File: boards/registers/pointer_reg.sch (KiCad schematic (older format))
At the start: 80 parts

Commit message: General-purpose register
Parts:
- U? (x4): value 74HC244 -> 74ACT244
- U? (x4): value 74LS161 -> 74ACT161
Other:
- note added: "The resistor values are such that each LED is driven by 10 mA (prevent 74ACT161 overload)."
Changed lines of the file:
@@
 $Descr A3 11693 16535 portrait
 encoding utf-8
-Sheet 3 4
+Sheet 3 6
 Title "Pointer register"
 Date "2019-12-28"
@@
 AR Path="/5E0666E8/5E5C90D9/5E067470" Ref="U?"  Part="1"
 F 0 "U?" H 5950 3250 50  0000 C CNN
-F 1 "74HC244" H 5850 3150 50  0000 C CNN
+F 1 "74ACT244" H 5850 3150 50  0000 C CNN
 F 2 "" H 5550 3850 50  0001 C CNN
 F 3 "https://assets.nexperia.com/documents/data-sheet/74HC_HCT244.pdf" H 5550 3850 50  0001 C CNN
@@
 AR Path="/5E0666E8/5E5C90D9/5E06F6F1" Ref="U?"  Part="1"
 F 0 "U?" H 8700 3200 50  0000 C CNN
-F 1 "74HC244" H 8600 3100 50  0000 C CNN
+F 1 "74ACT244" H 8600 3100 50  0000 C CNN
 F 2 "" H 8300 3850 50  0001 C CNN
 F 3 "https://assets.nexperia.com/documents/data-sheet/74HC_HCT244.pdf" H 8300 3850 50  0001 C CNN
@@
 AR Path="/5E0666E8/5E5C90D9/5E07142A" Ref="U?"  Part="1"
 F 0 "U?" H 5950 5900 50  0000 C CNN
-F 1 "74HC244" H 5850 5800 50  0000 C CNN
+F 1 "74ACT244" H 5850 5800 50  0000 C CNN
 F 2 "" H 5550 6500 50  0001 C CNN
 F 3 "https://assets.nexperia.com/documents/data-sheet/74HC_HCT244.pdf" H 5550 6500 50  0001 C CNN
@@
 AR Path="/5E0666E8/5E5C90D9/5E072984" Ref="U?"  Part="1"
 F 0 "U?" H 8650 5900 50  0000 C CNN
-F 1 "74HC244" H 8550 5800 50  0000 C CNN
+F 1 "74ACT244" H 8550 5800 50  0000 C CNN
 F 2 "" H 8250 6500 50  0001 C CNN
 F 3 "https://assets.nexperia.com/documents/data-sheet/74HC_HCT244.pdf" H 8250 6500 50  0001 C CNN
@@
 AR Path="/5E0666E8/5E5C90D9/5E0E2189" Ref="U?"  Part="1"
 F 0 "U?" H 4250 8700 50  0000 C CNN
-F 1 "74LS161" H 4150 8600 50  0000 C CNN
+F 1 "74ACT161" H 4150 8600 50  0000 C CNN
 F 2 "" H 3850 9250 50  0001 C CNN
 F 3 "http://www.ti.com/lit/gpn/sn74LS161" H 3850 9250 50  0001 C CNN
@@
 AR Path="/5E0666E8/5E5C90D9/5E0E857B" Ref="U?"  Part="1"
 F 0 "U?" H 4250 10850 50  0000 C CNN
-F 1 "74LS161" H 4150 10750 50  0000 C CNN
+F 1 "74ACT161" H 4150 10750 50  0000 C CNN
 F 2 "" H 3850 11400 50  0001 C CNN
 F 3 "http://www.ti.com/lit/gpn/sn74LS161" H 3850 11400 50  0001 C CNN
@@
 AR Path="/5E0666E8/5E5C90D9/5E0E941D" Ref="U?"  Part="1"
 F 0 "U?" H 6950 8700 50  0000 C CNN
-F 1 "74LS161" H 6850 8600 50  0000 C CNN
+F 1 "74ACT161" H 6850 8600 50  0000 C CNN
 F 2 "" H 6550 9250 50  0001 C CNN
 F 3 "http://www.ti.com/lit/gpn/sn74LS161" H 6550 9250 50  0001 C CNN
@@
 AR Path="/5E0666E8/5E5C90D9/5E0EB83E" Ref="U?"  Part="1"
 F 0 "U?" H 6950 10800 50  0000 C CNN
-F 1 "74LS161" H 6850 10700 50  0000 C CNN
+F 1 "74ACT161" H 6850 10700 50  0000 C CNN
 F 2 "" H 6550 11350 50  0001 C CNN
 F 3 "http://www.ti.com/lit/gpn/sn74LS161" H 6550 11350 50  0001 C CNN
@@
 Text Label 5100 14600 2    50   ~ 0
 lo7
+Text Notes 10700 13600 2    50   ~ 0
+The resistor values are such that each LED is driven by 10 mA (prevent 74ACT161 overload).
 $EndSCHEMATC

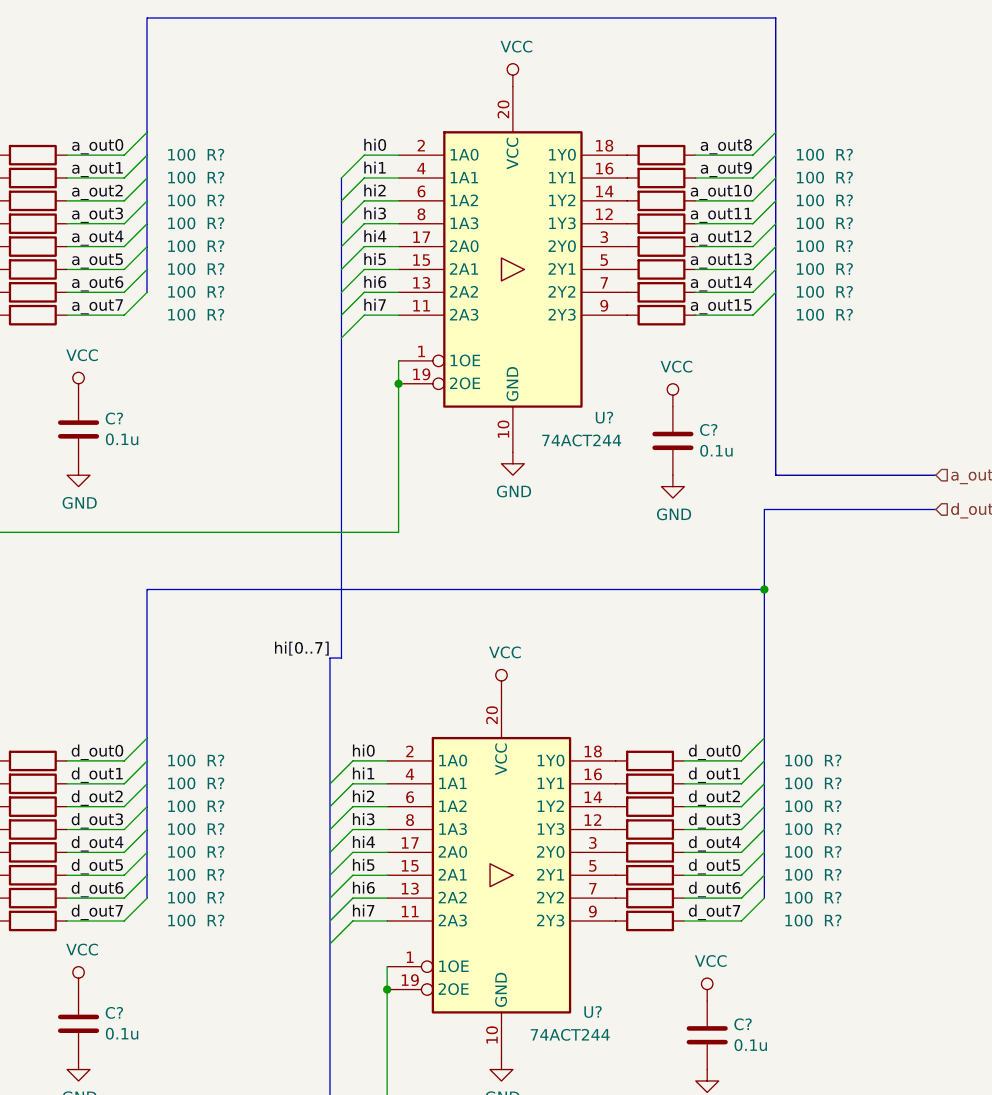
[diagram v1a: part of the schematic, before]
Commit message: Add bus resistors
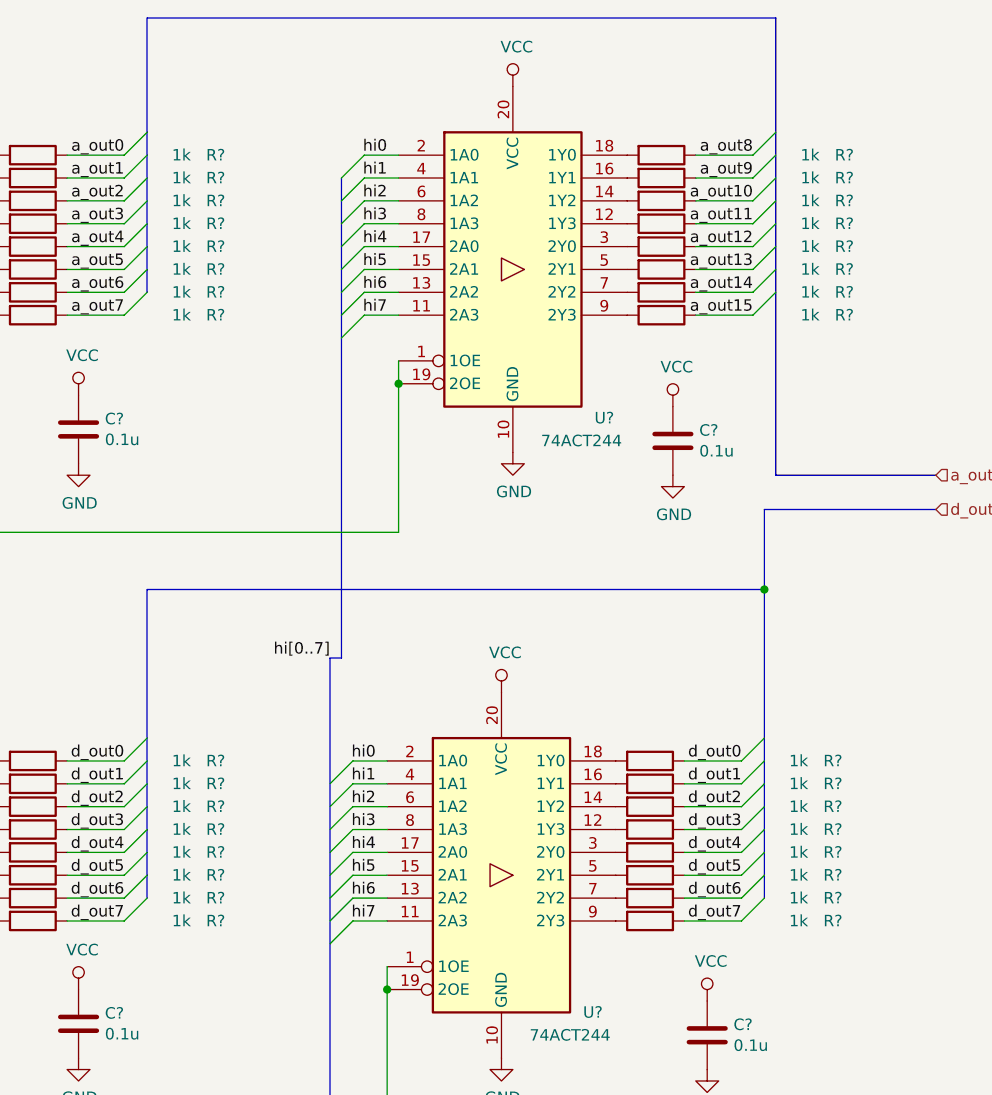
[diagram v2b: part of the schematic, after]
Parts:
- R? (x32): value 100 -> 1k
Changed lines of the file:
@@
 AR Path="/5E0666E8/5E5C90D9/5E079467" Ref="R?"  Part="1"
 F 0 "R?" V 6200 4150 50  0000 C CNN
-F 1 "100" V 6200 4000 50  0000 C CNN
+F 1 "1k" V 6200 4000 50  0000 C CNN
 F 2 "" V 6130 3350 50  0001 C CNN
 F 3 "~" H 6200 3350 50  0001 C CNN
@@
 AR Path="/5E0666E8/5E5C90D9/5E07A82D" Ref="R?"  Part="1"
 F 0 "R?" V 6200 4250 50  0000 C CNN
-F 1 "100" V 6200 4100 50  0000 C CNN
+F 1 "1k" V 6200 4100 50  0000 C CNN
 F 2 "" V 6130 3450 50  0001 C CNN
 F 3 "~" H 6200 3450 50  0001 C CNN
@@
 AR Path="/5E0666E8/5E5C90D9/5E07AA0F" Ref="R?"  Part="1"
 F 0 "R?" V 6200 4350 50  0000 C CNN
-F 1 "100" V 6200 4200 50  0000 C CNN
+F 1 "1k" V 6200 4200 50  0000 C CNN
 F 2 "" V 6130 3550 50  0001 C CNN
 F 3 "~" H 6200 3550 50  0001 C CNN
@@
 AR Path="/5E0666E8/5E5C90D9/5E07AB88" Ref="R?"  Part="1"
 F 0 "R?" V 6200 4450 50  0000 C CNN
-F 1 "100" V 6200 4300 50  0000 C CNN
+F 1 "1k" V 6200 4300 50  0000 C CNN
 F 2 "" V 6130 3650 50  0001 C CNN
 F 3 "~" H 6200 3650 50  0001 C CNN
@@
 AR Path="/5E0666E8/5E5C90D9/5E07AE3C" Ref="R?"  Part="1"
 F 0 "R?" V 6200 4550 50  0000 C CNN
-F 1 "100" V 6200 4400 50  0000 C CNN
+F 1 "1k" V 6200 4400 50  0000 C CNN
 F 2 "" V 6130 3750 50  0001 C CNN
 F 3 "~" H 6200 3750 50  0001 C CNN
@@
 AR Path="/5E0666E8/5E5C90D9/5E07B009" Ref="R?"  Part="1"
 F 0 "R?" V 6200 4650 50  0000 C CNN
-F 1 "100" V 6200 4500 50  0000 C CNN
+F 1 "1k" V 6200 4500 50  0000 C CNN
 F 2 "" V 6130 3850 50  0001 C CNN
 F 3 "~" H 6200 3850 50  0001 C CNN
@@
 AR Path="/5E0666E8/5E5C90D9/5E07B2BD" Ref="R?"  Part="1"
 F 0 "R?" V 6200 4750 50  0000 C CNN
-F 1 "100" V 6200 4600 50  0000 C CNN
+F 1 "1k" V 6200 4600 50  0000 C CNN
 F 2 "" V 6130 3950 50  0001 C CNN
 F 3 "~" H 6200 3950 50  0001 C CNN
@@
 AR Path="/5E0666E8/5E5C90D9/5E07B51D" Ref="R?"  Part="1"
 F 0 "R?" V 6200 4850 50  0000 C CNN
-F 1 "100" V 6200 4700 50  0000 C CNN
+F 1 "1k" V 6200 4700 50  0000 C CNN
 F 2 "" V 6130 4050 50  0001 C CNN
 F 3 "~" H 6200 4050 50  0001 C CNN
@@
 AR Path="/5E0666E8/5E5C90D9/5E07B83A" Ref="R?"  Part="1"
 F 0 "R?" V 8950 4150 50  0000 C CNN
-F 1 "100" V 8950 4000 50  0000 C CNN
+F 1 "1k" V 8950 4000 50  0000 C CNN
 F 2 "" V 8880 3350 50  0001 C CNN
 F 3 "~" H 8950 3350 50  0001 C CNN
@@
 AR Path="/5E0666E8/5E5C90D9/5E07C172" Ref="R?"  Part="1"
 F 0 "R?" V 8950 4250 50  0000 C CNN
-F 1 "100" V 8950 4100 50  0000 C CNN
+F 1 "1k" V 8950 4100 50  0000 C CNN
 F 2 "" V 8880 3450 50  0001 C CNN
 F 3 "~" H 8950 3450 50  0001 C CNN
@@
 AR Path="/5E0666E8/5E5C90D9/5E07C354" Ref="R?"  Part="1"
 F 0 "R?" V 8950 4350 50  0000 C CNN
-F 1 "100" V 8950 4200 50  0000 C CNN
+F 1 "1k" V 8950 4200 50  0000 C CNN
 F 2 "" V 8880 3550 50  0001 C CNN
 F 3 "~" H 8950 3550 50  0001 C CNN
@@
 AR Path="/5E0666E8/5E5C90D9/5E07C50C" Ref="R?"  Part="1"
 F 0 "R?" V 8950 4450 50  0000 C CNN
-F 1 "100" V 8950 4300 50  0000 C CNN
+F 1 "1k" V 8950 4300 50  0000 C CNN
 F 2 "" V 8880 3650 50  0001 C CNN
 F 3 "~" H 8950 3650 50  0001 C CNN
@@
 AR Path="/5E0666E8/5E5C90D9/5E07C6AF" Ref="R?"  Part="1"
 F 0 "R?" V 8950 4550 50  0000 C CNN
-F 1 "100" V 8950 4400 50  0000 C CNN
+F 1 "1k" V 8950 4400 50  0000 C CNN
 F 2 "" V 8880 3750 50  0001 C CNN
 F 3 "~" H 8950 3750 50  0001 C CNN
@@
 AR Path="/5E0666E8/5E5C90D9/5E07C852" Ref="R?"  Part="1"
 F 0 "R?" V 8950 4650 50  0000 C CNN
-F 1 "100" V 8950 4500 50  0000 C CNN
+F 1 "1k" V 8950 4500 50  0000 C CNN
 F 2 "" V 8880 3850 50  0001 C CNN
 F 3 "~" H 8950 3850 50  0001 C CNN
@@
 AR Path="/5E0666E8/5E5C90D9/5E07C9CB" Ref="R?"  Part="1"
 F 0 "R?" V 8950 4750 50  0000 C CNN
-F 1 "100" V 8950 4600 50  0000 C CNN
+F 1 "1k" V 8950 4600 50  0000 C CNN
 F 2 "" V 8880 3950 50  0001 C CNN
 F 3 "~" H 8950 3950 50  0001 C CNN
@@
 AR Path="/5E0666E8/5E5C90D9/5E07CCA9" Ref="R?"  Part="1"
 F 0 "R?" V 8950 4850 50  0000 C CNN
-F 1 "100" V 8950 4700 50  0000 C CNN
+F 1 "1k" V 8950 4700 50  0000 C CNN
 F 2 "" V 8880 4050 50  0001 C CNN
 F 3 "~" H 8950 4050 50  0001 C CNN
@@
 AR Path="/5E0666E8/5E5C90D9/5E07CEB5" Ref="R?"  Part="1"
 F 0 "R?" V 6200 6800 50  0000 C CNN
-F 1 "100" V 6200 6650 50  0000 C CNN
+F 1 "1k" V 6200 6650 50  0000 C CNN
 F 2 "" V 6130 6000 50  0001 C CNN
 F 3 "~" H 6200 6000 50  0001 C CNN
@@
 AR Path="/5E0666E8/5E5C90D9/5E07D90A" Ref="R?"  Part="1"
 F 0 "R?" V 6200 6900 50  0000 C CNN
-F 1 "100" V 6200 6750 50  0000 C CNN
+F 1 "1k" V 6200 6750 50  0000 C CNN
 F 2 "" V 6130 6100 50  0001 C CNN
 F 3 "~" H 6200 6100 50  0001 C CNN
@@
 AR Path="/5E0666E8/5E5C90D9/5E07DC66" Ref="R?"  Part="1"
 F 0 "R?" V 6200 7000 50  0000 C CNN
-F 1 "100" V 6200 6850 50  0000 C CNN
+F 1 "1k" V 6200 6850 50  0000 C CNN
 F 2 "" V 6130 6200 50  0001 C CNN
 F 3 "~" H 6200 6200 50  0001 C CNN
@@
 AR Path="/5E0666E8/5E5C90D9/5E07DE33" Ref="R?"  Part="1"
 F 0 "R?" V 6200 7100 50  0000 C CNN
-F 1 "100" V 6200 6950 50  0000 C CNN
+F 1 "1k" V 6200 6950 50  0000 C CNN
 F 2 "" V 6130 6300 50  0001 C CNN
 F 3 "~" H 6200 6300 50  0001 C CNN
@@
 AR Path="/5E0666E8/5E5C90D9/5E07E093" Ref="R?"  Part="1"
 F 0 "R?" V 6200 7200 50  0000 C CNN
-F 1 "100" V 6200 7050 50  0000 C CNN
+F 1 "1k" V 6200 7050 50  0000 C CNN
 F 2 "" V 6130 6400 50  0001 C CNN
 F 3 "~" H 6200 6400 50  0001 C CNN
@@
 AR Path="/5E0666E8/5E5C90D9/5E07E347" Ref="R?"  Part="1"
 F 0 "R?" V 6200 7300 50  0000 C CNN
-F 1 "100" V 6200 7150 50  0000 C CNN
+F 1 "1k" V 6200 7150 50  0000 C CNN
 F 2 "" V 6130 6500 50  0001 C CNN
 F 3 "~" H 6200 6500 50  0001 C CNN
@@
 AR Path="/5E0666E8/5E5C90D9/5E07E64F" Ref="R?"  Part="1"
 F 0 "R?" V 6200 7400 50  0000 C CNN
-F 1 "100" V 6200 7250 50  0000 C CNN
+F 1 "1k" V 6200 7250 50  0000 C CNN
 F 2 "" V 6130 6600 50  0001 C CNN
 F 3 "~" H 6200 6600 50  0001 C CNN
@@
 AR Path="/5E0666E8/5E5C90D9/5E07E7C8" Ref="R?"  Part="1"
 F 0 "R?" V 6200 7500 50  0000 C CNN
-F 1 "100" V 6200 7350 50  0000 C CNN
+F 1 "1k" V 6200 7350 50  0000 C CNN
 F 2 "" V 6130 6700 50  0001 C CNN
 F 3 "~" H 6200 6700 50  0001 C CNN
@@
 AR Path="/5E0666E8/5E5C90D9/5E07E941" Ref="R?"  Part="1"
 F 0 "R?" V 8900 6800 50  0000 C CNN
-F 1 "100" V 8900 6650 50  0000 C CNN
+F 1 "1k" V 8900 6650 50  0000 C CNN
 F 2 "" V 8830 6000 50  0001 C CNN
 F 3 "~" H 8900 6000 50  0001 C CNN
@@
 AR Path="/5E0666E8/5E5C90D9/5E07F04E" Ref="R?"  Part="1"
 F 0 "R?" V 8900 6900 50  0000 C CNN
-F 1 "100" V 8900 6750 50  0000 C CNN
+F 1 "1k" V 8900 6750 50  0000 C CNN
 F 2 "" V 8830 6100 50  0001 C CNN
 F 3 "~" H 8900 6100 50  0001 C CNN
@@
 AR Path="/5E0666E8/5E5C90D9/5E07F2D8" Ref="R?"  Part="1"
 F 0 "R?" V 8900 7000 50  0000 C CNN
-F 1 "100" V 8900 6850 50  0000 C CNN
+F 1 "1k" V 8900 6850 50  0000 C CNN
 F 2 "" V 8830 6200 50  0001 C CNN
 F 3 "~" H 8900 6200 50  0001 C CNN
@@
 AR Path="/5E0666E8/5E5C90D9/5E07F490" Ref="R?"  Part="1"
 F 0 "R?" V 8900 7100 50  0000 C CNN
-F 1 "100" V 8900 6950 50  0000 C CNN
+F 1 "1k" V 8900 6950 50  0000 C CNN
 F 2 "" V 8830 6300 50  0001 C CNN
 F 3 "~" H 8900 6300 50  0001 C CNN
@@
 AR Path="/5E0666E8/5E5C90D9/5E07F72F" Ref="R?"  Part="1"
 F 0 "R?" V 8900 7200 50  0000 C CNN
-F 1 "100" V 8900 7050 50  0000 C CNN
+F 1 "1k" V 8900 7050 50  0000 C CNN
 F 2 "" V 8830 6400 50  0001 C CNN
 F 3 "~" H 8900 6400 50  0001 C CNN
@@
 AR Path="/5E0666E8/5E5C90D9/5E07F9CE" Ref="R?"  Part="1"
 F 0 "R?" V 8900 7300 50  0000 C CNN
-F 1 "100" V 8900 7150 50  0000 C CNN
+F 1 "1k" V 8900 7150 50  0000 C CNN
 F 2 "" V 8830 6500 50  0001 C CNN
 F 3 "~" H 8900 6500 50  0001 C CNN
@@
 AR Path="/5E0666E8/5E5C90D9/5E07FB5C" Ref="R?"  Part="1"
 F 0 "R?" V 8900 7400 50  0000 C CNN
-F 1 "100" V 8900 7250 50  0000 C CNN
+F 1 "1k" V 8900 7250 50  0000 C CNN
 F 2 "" V 8830 6600 50  0001 C CNN
 F 3 "~" H 8900 6600 50  0001 C CNN
@@
 AR Path="/5E0666E8/5E5C90D9/5E07FDBC" Ref="R?"  Part="1"
 F 0 "R?" V 8900 7500 50  0000 C CNN
-F 1 "100" V 8900 7350 50  0000 C CNN
+F 1 "1k" V 8900 7350 50  0000 C CNN
 F 2 "" V 8830 6700 50  0001 C CNN
 F 3 "~" H 8900 6700 50  0001 C CNN

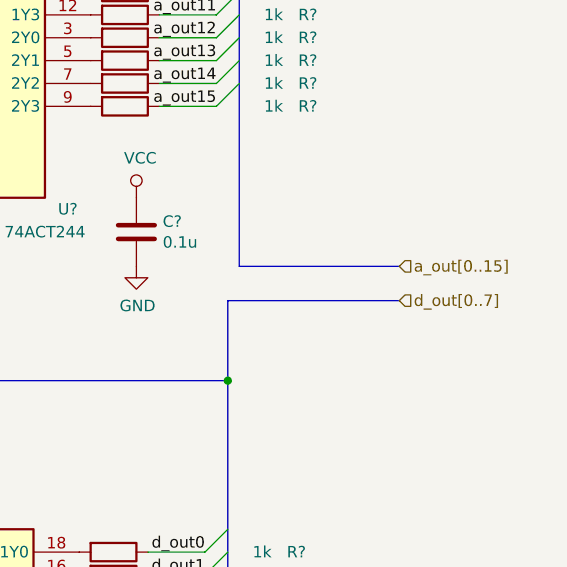
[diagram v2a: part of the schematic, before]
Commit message: Remove redundant chip from the register A, change hierarchical pin types
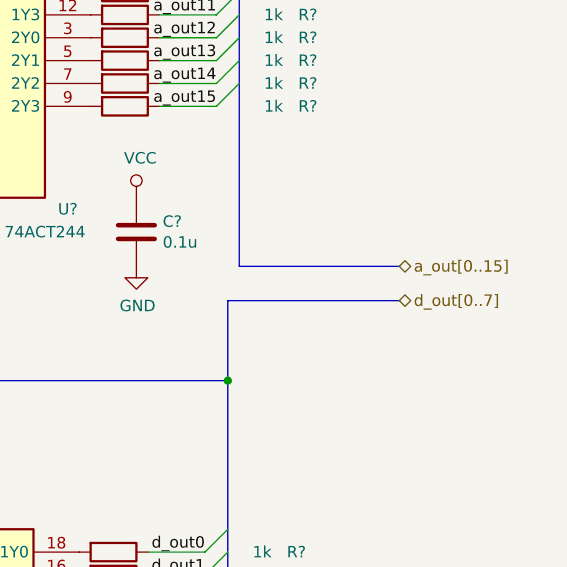
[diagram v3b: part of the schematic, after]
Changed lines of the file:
@@
 $Descr A3 11693 16535 portrait
 encoding utf-8
-Sheet 3 6
+Sheet 3 7
 Title "Pointer register"
 Date "2019-12-28"
@@
 Text HLabel 1500 5150 0    50   Input ~ 0
 ~oe_dl
-Text HLabel 10150 4750 2    50   Input ~ 0
+Text HLabel 10150 4750 2    50   3State ~ 0
 a_out[0..15]
-Text HLabel 10150 4900 2    50   Input ~ 0
+Text HLabel 10150 4900 2    50   3State ~ 0
 d_out[0..7]
 $Comp
